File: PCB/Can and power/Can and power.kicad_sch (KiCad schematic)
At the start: 32 parts, among them IC1 MCP2515-e_ST, IC2 TJA1044VT_3Z, J1 TPS54232DR, J2 ESP32, J3 12V, J4 C_H, J5 C_L, J6 GND, Y1 16MHz

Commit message: Pre-traces
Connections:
- net GND: now also R4.1; no longer C7.2
- net at C7.1: now also C8.1, J1.6 (COMP); no longer R4.1
- new net: C7.2, R4.2
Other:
- moved on the sheet: C7, R4

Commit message: First purchase
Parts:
- C1, C2: Manufacturer_Name (none) -> KEMET; Manufacturer_Part_Number (none) -> C0603C220K4GAC7867
- C10, C3, C4, C5: value 100n -> 0.1uF; Manufacturer_Name (none) -> YAGEO; Manufacturer_Part_Number (none) -> CC0603KRX7R7BB104
- C11: value 10u -> 10uF; Manufacturer_Name (none) -> SAMSUNG; Manufacturer_Part_Number (none) -> CL10A106KP8NNNC
- C6: value 8n2 -> 8200pF; Manufacturer_Name (none) -> KEMET; Manufacturer_Part_Number (none) -> C0603C822J3GAC7867
- C7: value 4n7 -> 4700pF; Manufacturer_Name (none) -> KEMET; Manufacturer_Part_Number (none) -> C0603C472K4RAC7867
- C8: value 110p -> 100pF; Manufacturer_Name (none) -> KYOCERA AVX; Manufacturer_Part_Number (none) -> KGM15AR71C101KT
- C9: Manufacturer_Name (none) -> SAMSUNG; Manufacturer_Part_Number (none) -> CL31B106KAHNNNE
- J2, J3, J4, J5, J6: now left out of the parts list
- R1, R11, R2, R7, R9: Manufacturer_Name (none) -> YAGEO; Manufacturer_Part_Number (none) -> RC0603FR-0710K2L
- R10: Manufacturer_Name (none) -> YAGEO; Manufacturer_Part_Number (none) -> RC0603FR-071K91L
- R4: Manufacturer_Name (none) -> YAGEO; Manufacturer_Part_Number (none) -> RC0603FR-0712K7L
- R8: Manufacturer_Name (none) -> Stackpole; Manufacturer_Part_Number (none) -> RMCF0603ZT0R00
- Y1: Manufacturer_Name (none) -> EPSON; Manufacturer_Part_Number (none) -> TSX-3225 16.0000MF09Z-AC0

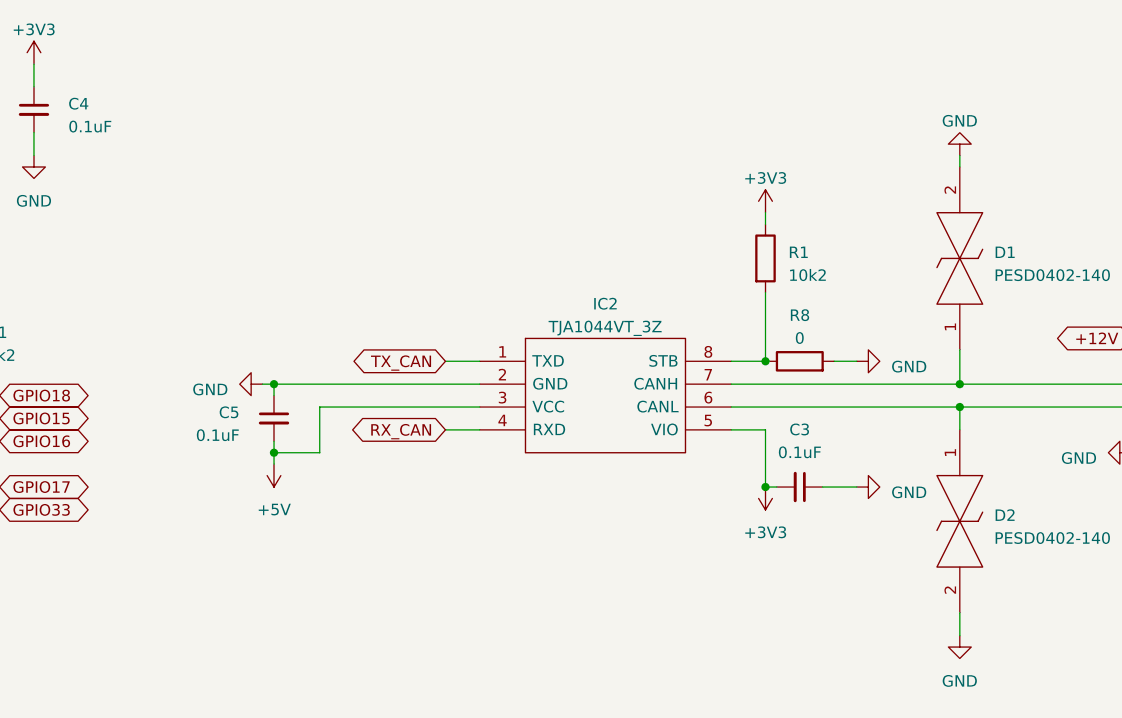
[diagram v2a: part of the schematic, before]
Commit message: Change of transceiver
For some reasons the TJA 1044 and 1049 get stuck in Standby mode all the time. Not sure why.
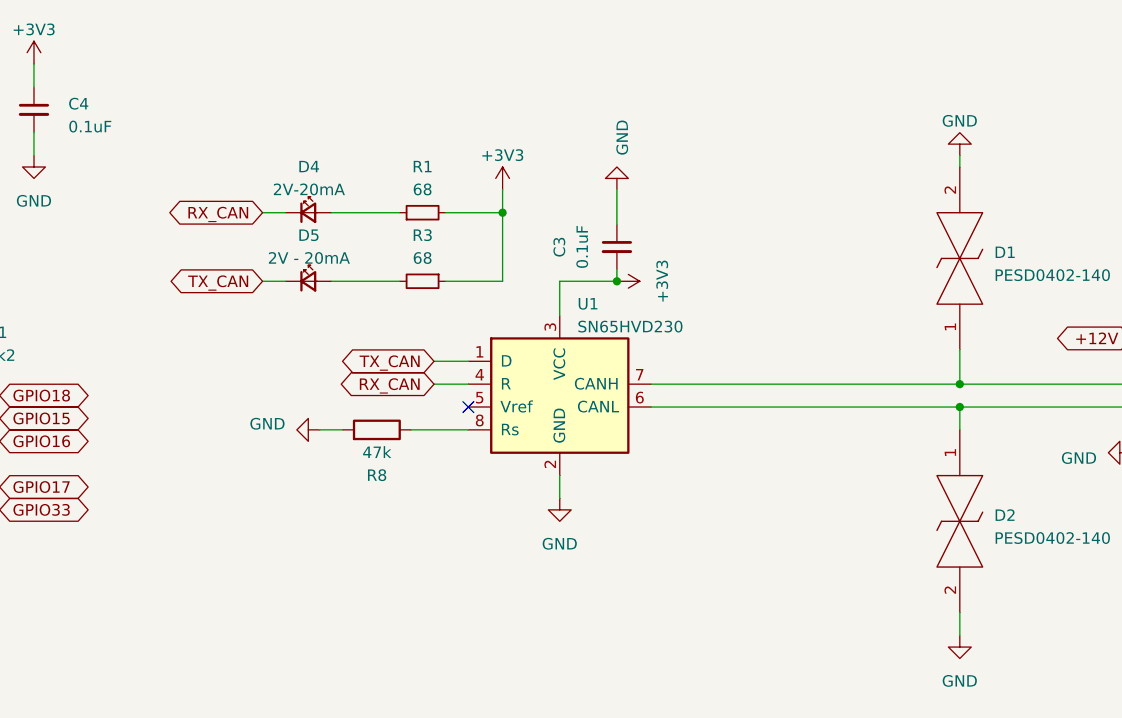
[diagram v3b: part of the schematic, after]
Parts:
- removed C5: 0.1uF, Capacitor_SMD:C_0603_1608Metric, symbol Device:C_Small
- removed IC2: TJA1044VT_3Z, SamacSys_Parts:SOIC127P600X175-8N, symbol SamacSys_Parts:TJA1044VT_3Z
- removed R1: 10k2, Resistor_SMD:R_0603_1608Metric, symbol Device:R
- added D4: 2V-20mA, LED_SMD:LED_0603_1608Metric, symbol Device:LED_Small
- added D5: 2V - 20mA, LED_SMD:LED_0603_1608Metric, symbol Device:LED_Small
- added R1, R3: 68, Resistor_SMD:R_0603_1608Metric, symbol Device:R_Small
- added U1: SN65HVD230, Package_SO:SOIC-8_3.9x4.9mm_P1.27mm, symbol Interface_CAN_LIN:SN65HVD230
- R8: value 0 -> 47k; Manufacturer_Name Stackpole -> Panasonic Electronic Components; Manufacturer_Part_Number RMCF0603ZT0R00 -> ERJ-3EKF4702V
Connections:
- net +3V3: now also R1.2, R3.1, U1.3 (VCC)
- net GND: now also U1.2 (GND)
- net RX_CAN: now also D4.1 (K), U1.4 (R)
- net TX_CAN: now also D5.1 (K), U1.1 (D)
- net at D2.1, J5.1 (Pin_1): now also U1.6 (CANL)
- net at D1.1, J4.1 (Pin_1): now also U1.7 (CANH)
- net at R8.1: now also U1.8 (Rs)
- new net: D4.2 (A), R1.1
- new net: D5.2 (A), R3.2
- no-connect marks 10 -> 11
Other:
- moved on the sheet: C3

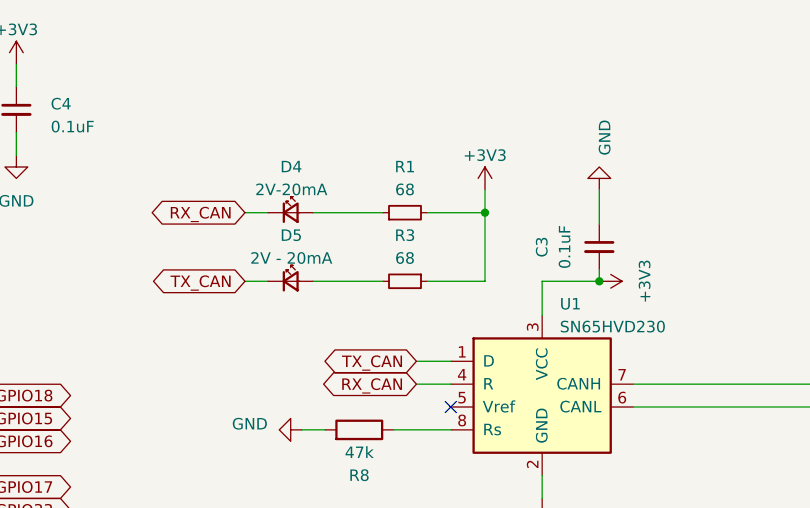
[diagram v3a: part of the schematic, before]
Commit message: LED resistor corrections
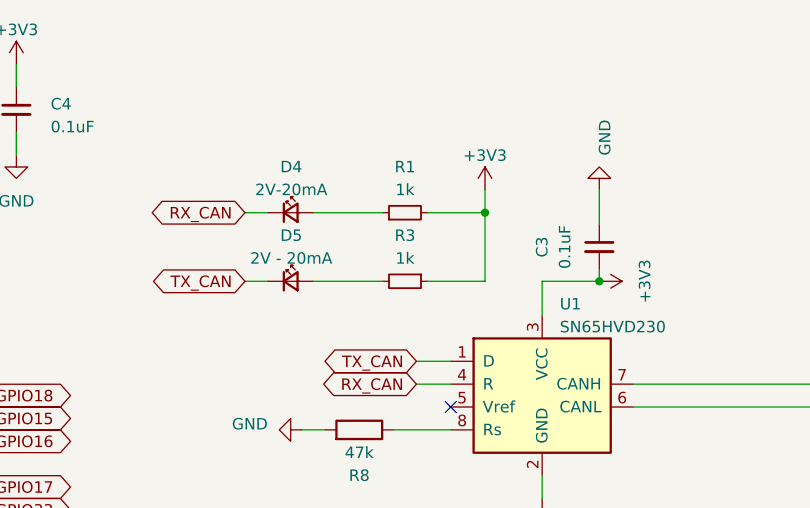
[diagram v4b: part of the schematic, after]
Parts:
- R1, R3: value 68 -> 1k; Manufacturer_Part_Number RC0603FR-0768RL -> RC0603FR-071KL
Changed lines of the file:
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@@
       (effects (font (size 1.27 1.27)))
     )
-    (property "Value" "68" (at 176.53 45.72 90)
+    (property "Value" "1k" (at 176.53 45.72 90)
       (effects (font (size 1.27 1.27)))
     )
@@
       (effects (font (size 1.27 1.27)) hide)
     )
-    (property "Description" "RES 68 OHM 1% 1/10W 0603" (at 176.53 48.26 0)
+    (property "Description" "RES 1K OHM 1% 1/10W 0603" (at 176.53 48.26 0)
       (effects (font (size 1.27 1.27)) hide)
     )
@@
       (effects (font (size 1.27 1.27)) hide)
     )
-    (property "Manufacturer_Part_Number" "RC0603FR-0768RL" (at 176.53 48.26 0)
+    (property "Manufacturer_Part_Number" "RC0603FR-071KL" (at 176.53 48.26 0)
       (effects (font (size 1.27 1.27)) hide)
     )
@@
       (effects (font (size 1.27 1.27)))
     )
-    (property "Value" "68" (at 176.53 53.34 90)
+    (property "Value" "1k" (at 176.53 53.34 90)
       (effects (font (size 1.27 1.27)))
     )
@@
       (effects (font (size 1.27 1.27)) hide)
     )
-    (property "Description" "RES 68 OHM 1% 1/10W 0603" (at 176.53 55.88 0)
+    (property "Description" "RES 1K OHM 1% 1/10W 0603" (at 176.53 55.88 0)
       (effects (font (size 1.27 1.27)) hide)
     )
@@
       (effects (font (size 1.27 1.27)) hide)
     )
-    (property "Manufacturer_Part_Number" "RC0603FR-0768RL" (at 176.53 55.88 0)
-      (effects (font (size 1.27 1.27)) hide)
-    )
+    (property "Manufacturer_Part_Number" "RC0603FR-071KL" (at 176.53 55.88 0)
+      (effects (font (size 1.27 1.27)) hide)
+    )

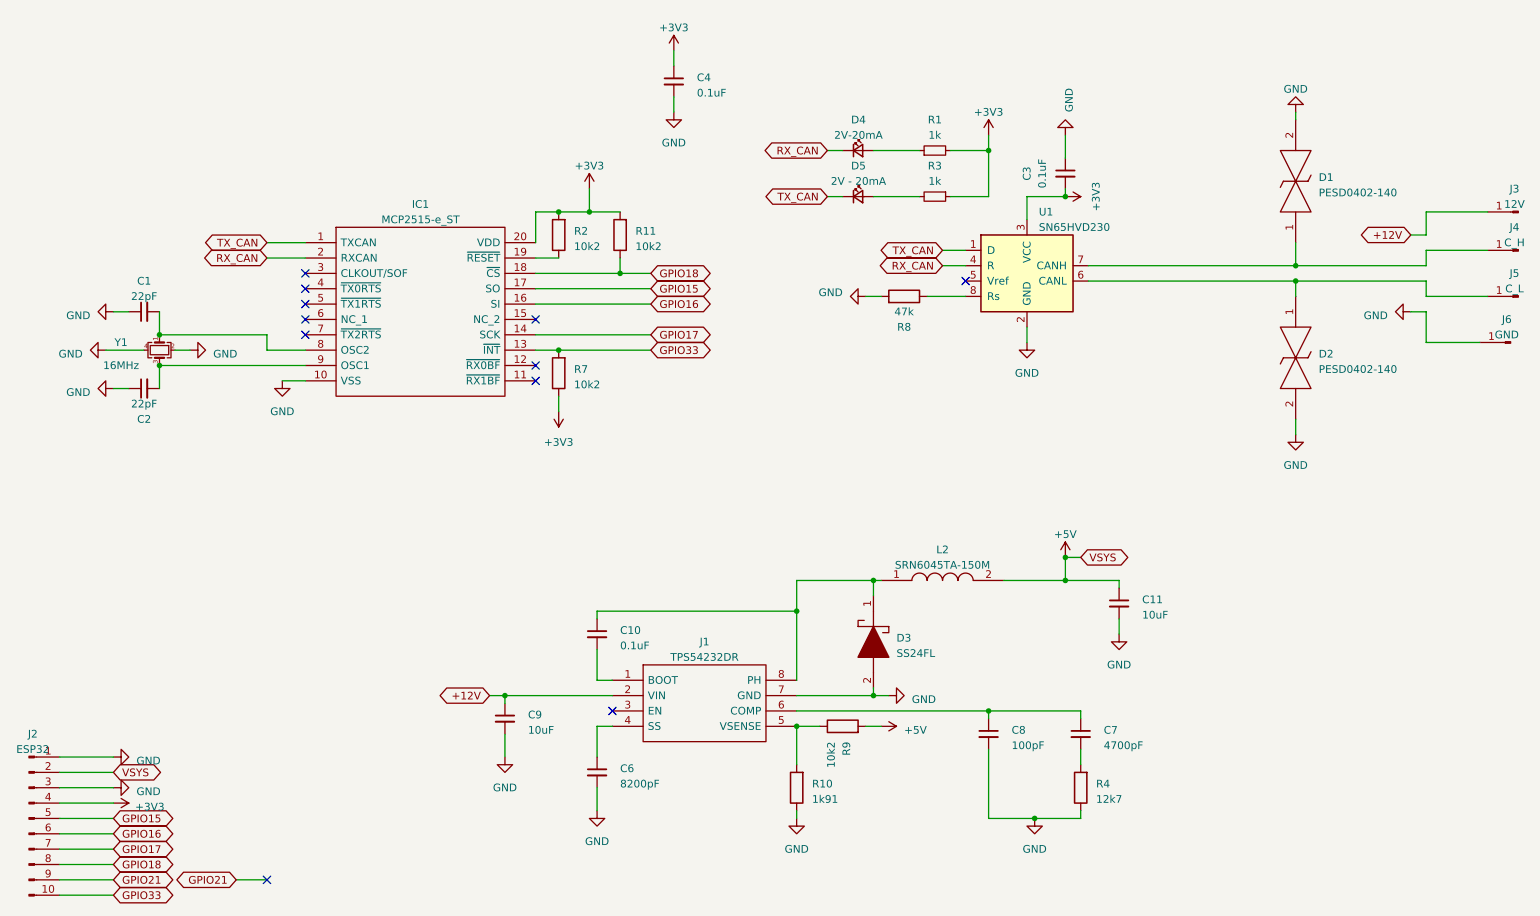
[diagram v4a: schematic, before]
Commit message: Clean-up code and sch, PCB layout is a WIP
Code limited to TWAI implementation
Schematic updated with solder bridges
PCB layout is a WIP
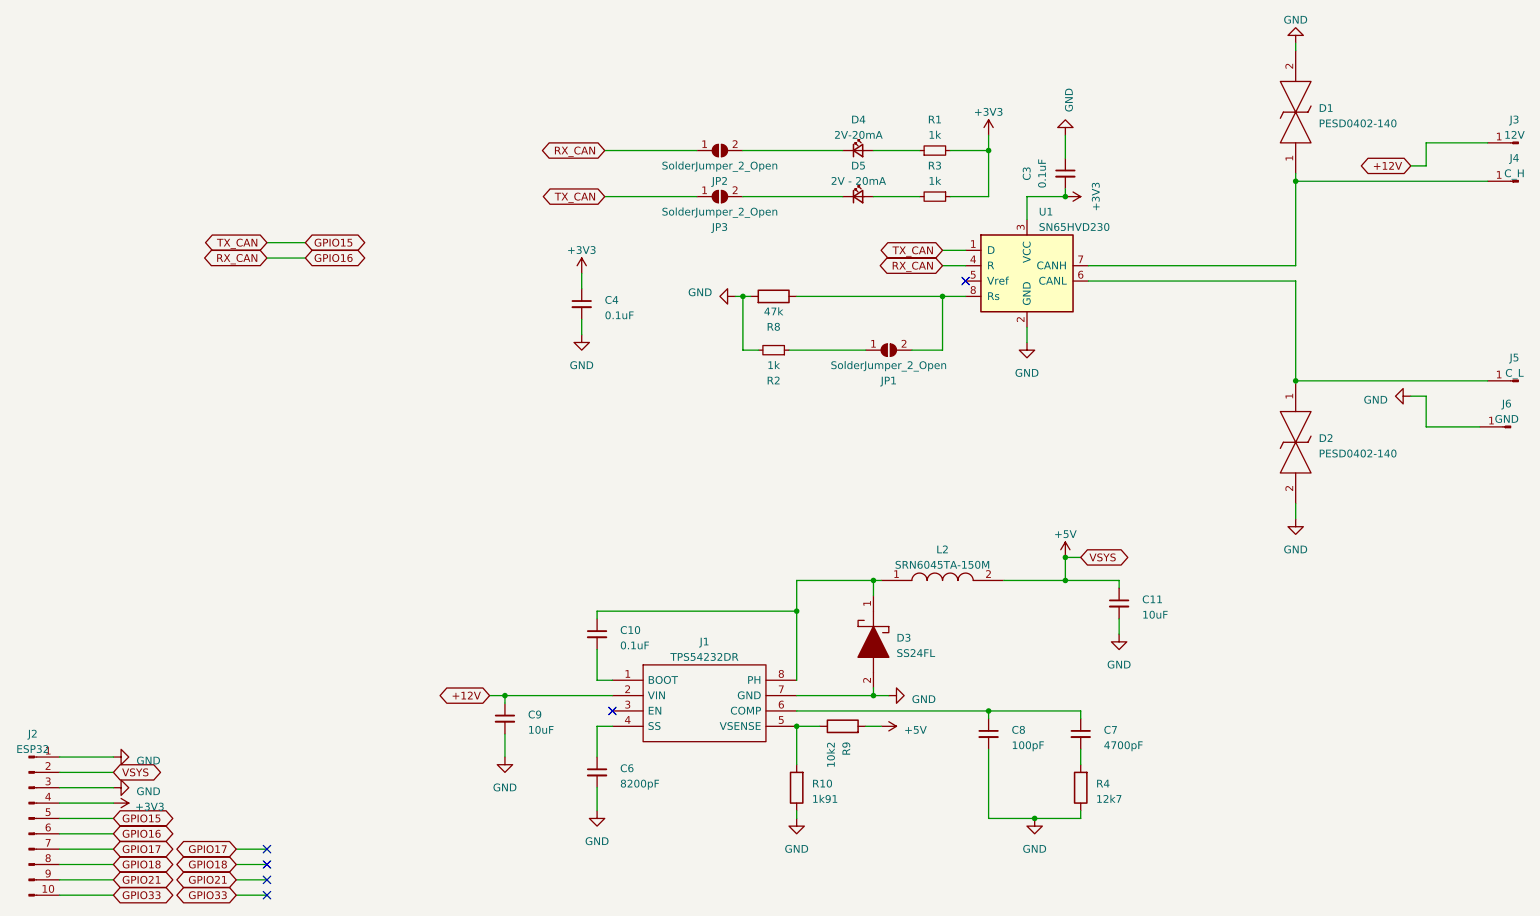
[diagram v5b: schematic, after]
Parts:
- removed C1, C2: 22pF, Capacitor_SMD:C_0603_1608Metric, symbol Device:C_Small
- removed IC1: MCP2515-e_ST, SamacSys_Parts:SOP65P640X120-20N, symbol SamacSys_Parts:MCP2515-e_ST
- removed R11, R2, R7: 10k2, Resistor_SMD:R_0603_1608Metric, symbol Device:R
- removed Y1: 16MHz, Crystal:Crystal_SMD_3225-4Pin_3.2x2.5mm, symbol Device:Crystal_GND24_Small
- added JP1, JP2, JP3: SolderJumper_2_Open, Jumper:SolderJumper-2_P1.3mm_Open_RoundedPad1.0x1.5mm, symbol Jumper:SolderJumper_2_Open
- added R2: 1k, Resistor_SMD:R_0603_1608Metric, symbol Device:R_Small
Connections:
- net GND: now also R2.2
- net GPIO15: now also U1.1 (D), JP3.1 (A)
- net GPIO16: now also U1.4 (R), JP2.1 (A)
- net at R8.1, U1.8 (Rs): now also JP1.2 (B)
- net RX_CAN: no longer names the net of D4.1 (K)
- net RX_CAN: now also JP2.2 (B); no longer U1.4 (R)
- net TX_CAN: no longer names the net of D5.1 (K)
- net TX_CAN: now also JP3.2 (B); no longer U1.1 (D)
- new net: JP1.1 (A), R2.1
- no-connect marks 11 -> 6
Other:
- moved on the sheet: C4, D1, D2, J3, J4, J5, J6, R8
